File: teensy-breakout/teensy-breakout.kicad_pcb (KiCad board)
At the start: 6 copper layers, 139.7 x 133.4 mm, 80 parts, among them J1 USB_B, J10 Conn_01x04, J11 Conn_01x04, J12 Conn_01x05, J13 Conn_01x03, J14 Conn_01x04, J15 Conn_01x04, J16 Conn_01x02, J17 Conn_01x08, J18 Conn_01x08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

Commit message: Added most of the silkscreen
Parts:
- added G***: LOGO, LOGO, F.Cu at (213.4, 240.0)
- added G***: LOGO, LOGO, F.Cu at (168.9, 212.1)
- added G***: LOGO, LOGO, F.Cu at (189.2, 212.1)
- added REF**: MountingHole_3.2mm_M3, MountingHole:MountingHole_3.2mm_M3, F.Cu at (104.1, 261.6)
- added REF**: MountingHole_3.2mm_M3, MountingHole:MountingHole_3.2mm_M3, F.Cu at (227.3, 172.7)
- added REF**: MountingHole_3.2mm_M3, MountingHole:MountingHole_3.2mm_M3, F.Cu at (227.3, 261.6)
- added REF**: MountingHole_3.2mm_M3, MountingHole:MountingHole_3.2mm_M3, F.Cu at (227.3, 148.6)
- moved J10 5.08 mm to (195.6, 226.1)
- moved J19 3.81 mm to (121.9, 151.1)
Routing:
- net /RC_TX: track 83.8 -> 88.9 mm
- net /RC_RX: track 85.3 -> 90.4 mm
- net /NP1_5V: track 17.1 -> 17.6 mm
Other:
- board text added: "+5V"
- board text added: "4"
- board text added: "5"
- board text added: "GND"
- board text added: "MISO0 12"
- board text added: "MOSI0 11"
- board text added: "SCK0 13"

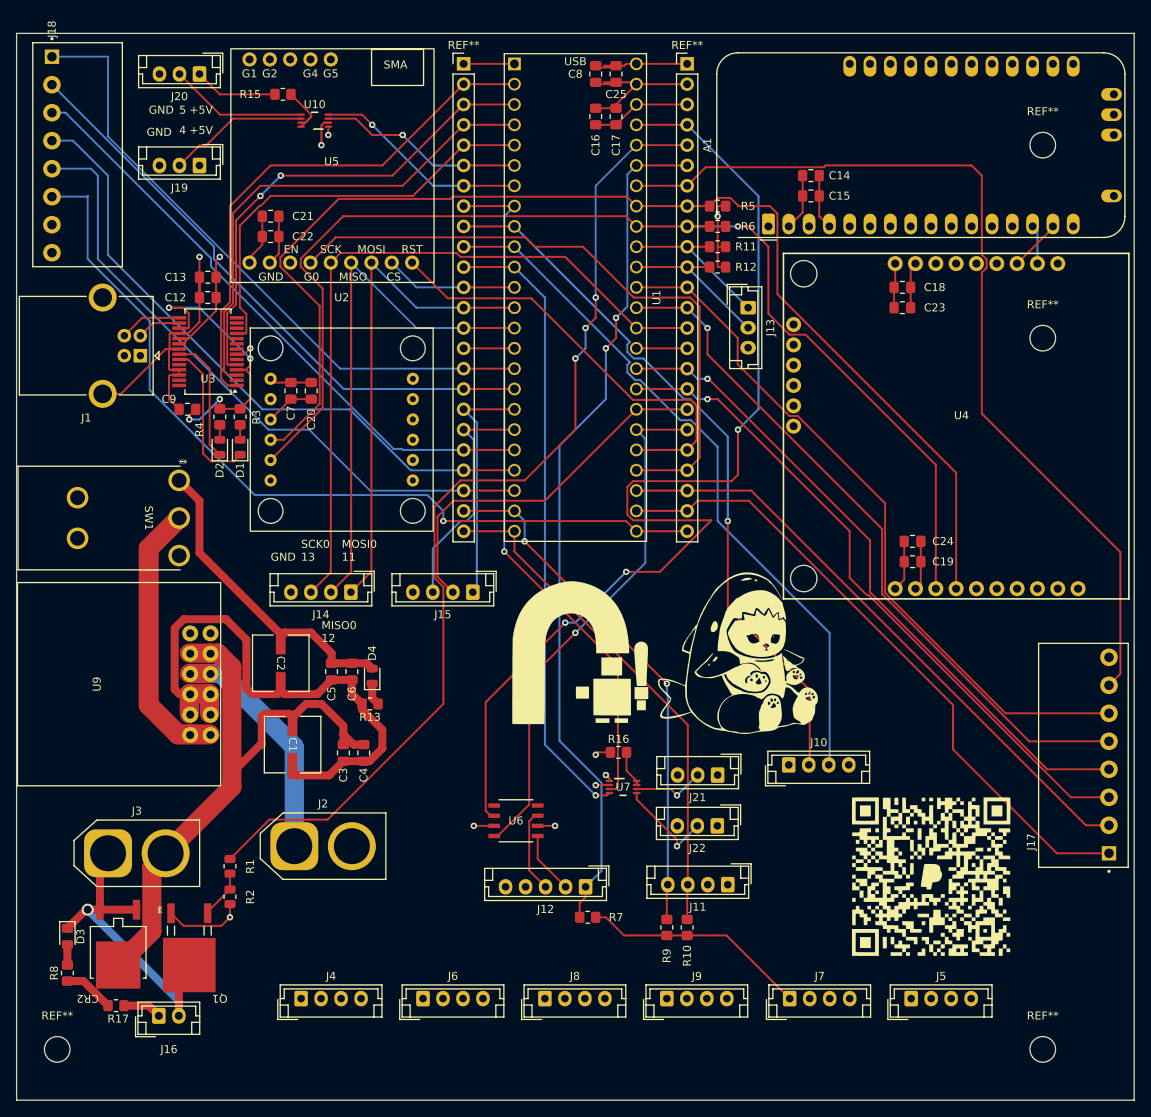
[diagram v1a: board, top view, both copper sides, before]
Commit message: Added rest of silkscreen
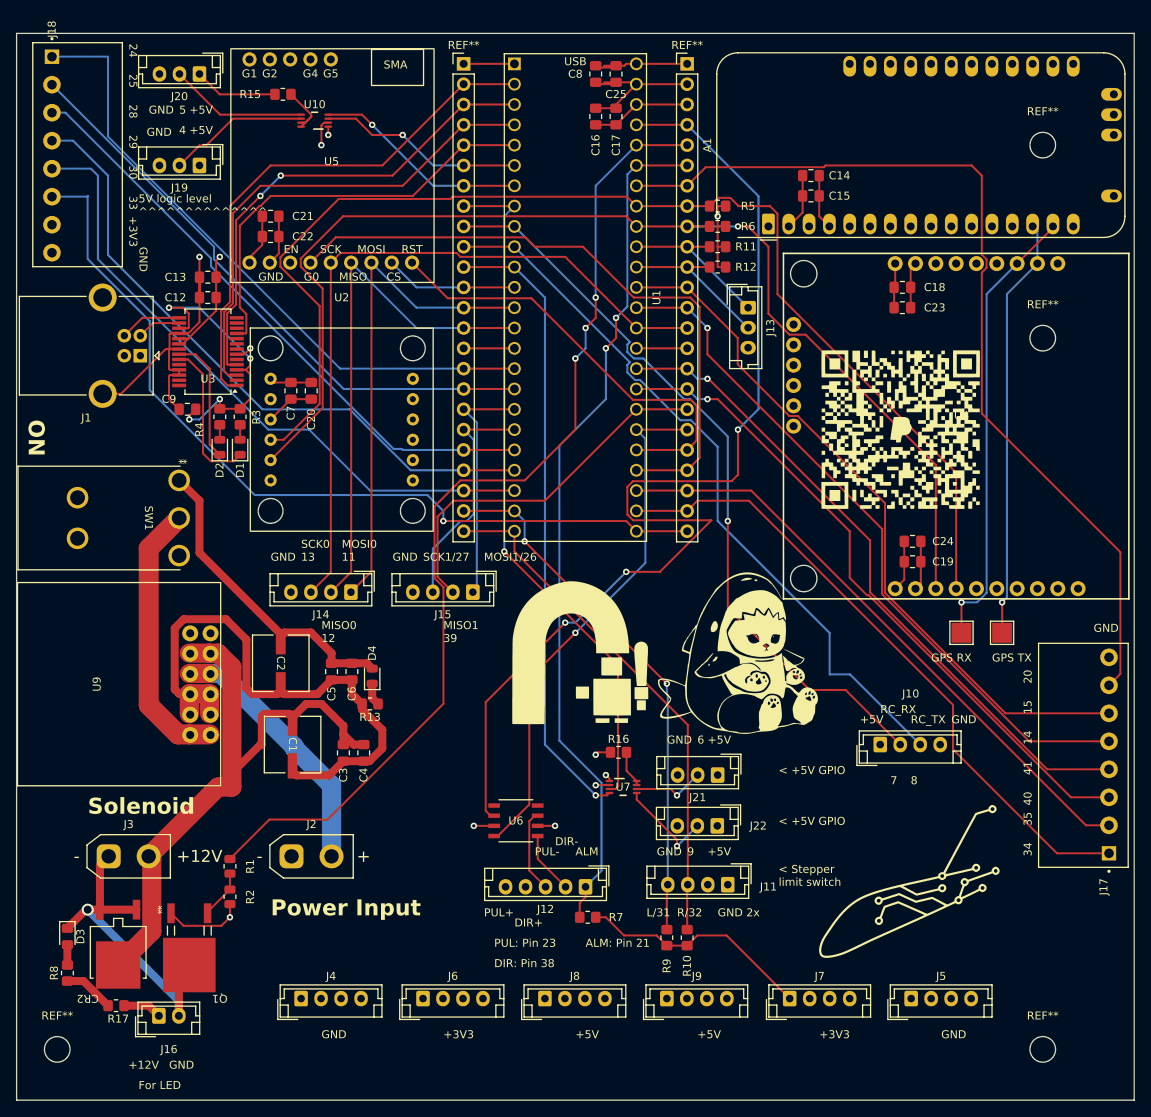
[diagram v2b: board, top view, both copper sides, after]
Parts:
- added G***: LOGO, LOGO, F.Cu at (210.8, 241.3)
- added REF**: TestPoint_Pad_2.5x2.5mm, TestPoint:TestPoint_Pad_2.5x2.5mm, F.Cu at (222.2, 209.6)
- added REF**: TestPoint_Pad_2.5x2.5mm, TestPoint:TestPoint_Pad_2.5x2.5mm, F.Cu at (217.2, 209.6)
- J2, J3: footprint Connector_AMASS:AMASS_XT60-F_1x02_P7.20mm_Vertical -> Connector_AMASS:AMASS_XT30UPB-M_1x02_P5.0mm_Vertical
- moved G*** 56.0 mm to (209.6, 184.2)
- moved J10 11.7 mm to (207.0, 223.5)
- moved J2 1.31 mm to (133.4, 237.5)
- moved R10 1.27 mm to (182.9, 247.7)
- moved R9 1.27 mm to (180.3, 247.7)
- moved J3 0.39 mm to (110.6, 237.5)
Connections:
- J2 pad 1: Net-(J2-Pin_1) -> GND
- J2 pad 2: GND -> Net-(J2-Pin_2)
- U9 pad 4: Net-(J2-Pin_1) -> Net-(J2-Pin_2)
- U9 pad 9: Net-(J2-Pin_1) -> Net-(J2-Pin_2)
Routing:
- net /GPS_RX: track 6.50 -> 56.7 mm, vias 0 -> 1
- net /GPS_TX: track 4.89 -> 52.9 mm, vias 0 -> 1
- net Net-(J2-Pin_2): track 0.00 -> 32.5 mm
- net Net-(J2-Pin_1): track 29.3 -> 0.00 mm
- net /RC_RX: track 90.4 -> 95.2 mm
- net /RC_TX: track 88.9 -> 92.5 mm
- net +12V: track 84.5 -> 85.8 mm
- net /LIM_R: track 63.9 -> 65.2 mm
- net /LIM_L: track 65.4 -> 66.7 mm
- net +3V3: track 89.1 -> 90.2 mm
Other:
- board text added: "+12V"
- board text added: "+3V3"
- board text added: "14"
- board text added: "15"
- board text added: "20"
- board text added: "24"
- board text added: "25"
- board text added: "28"
- board text added: "29"
- board text added: "30"
- board text added: "33"
- board text added: "34"
- board text added: "35"
- board text added: "40"
- board text added: "41"
- board text added: "5V logic level ^^^^^^^^^^^^^^"
- board text added: "6"
- board text added: "7"
- board text added: "8"
- board text added: "9"
- board text added: "< +5V GPIO"
- board text added: "< Stepper limit switch"
- board text added: "ALM"
- board text added: "ALM: Pin 21"
- board text added: "DIR+"
- board text added: "DIR-"
- board text added: "DIR: Pin 38"
- board text added: "For LED"
- board text added: "GND 2x"
- board text added: "GPS RX"
- board text added: "GPS TX"
- board text added: "L/31"
- board text added: "MISO1 39"
- board text added: "MOSI1/26"
- board text added: "ON"
- board text added: "PUL+"
- board text added: "PUL-"
- board text added: "PUL: Pin 23"
- board text added: "Power Input"
- board text added: "R/32"
- board text added: "RC_RX"
- board text added: "RC_TX"
- board text added: "SCK1/27"
- board text added: "Solenoid"

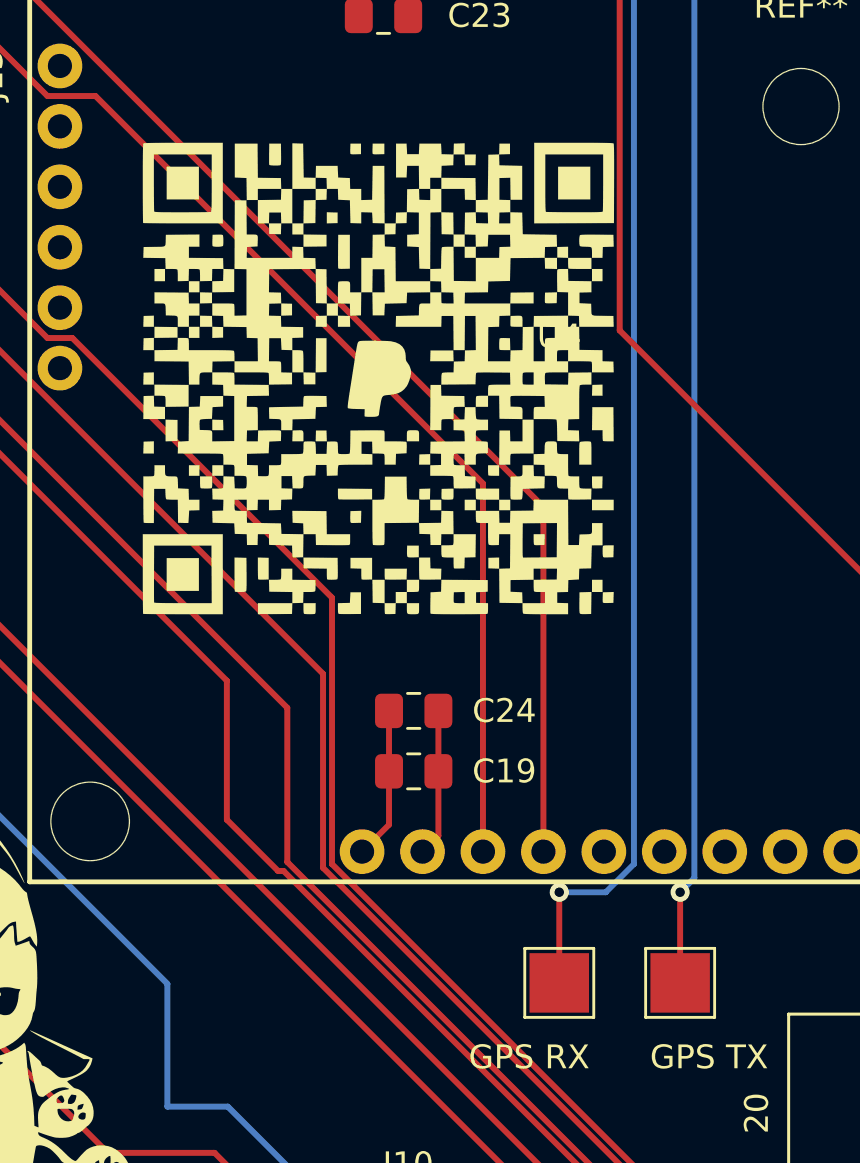
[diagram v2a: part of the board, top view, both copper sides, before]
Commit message: Fixed DRC warnings
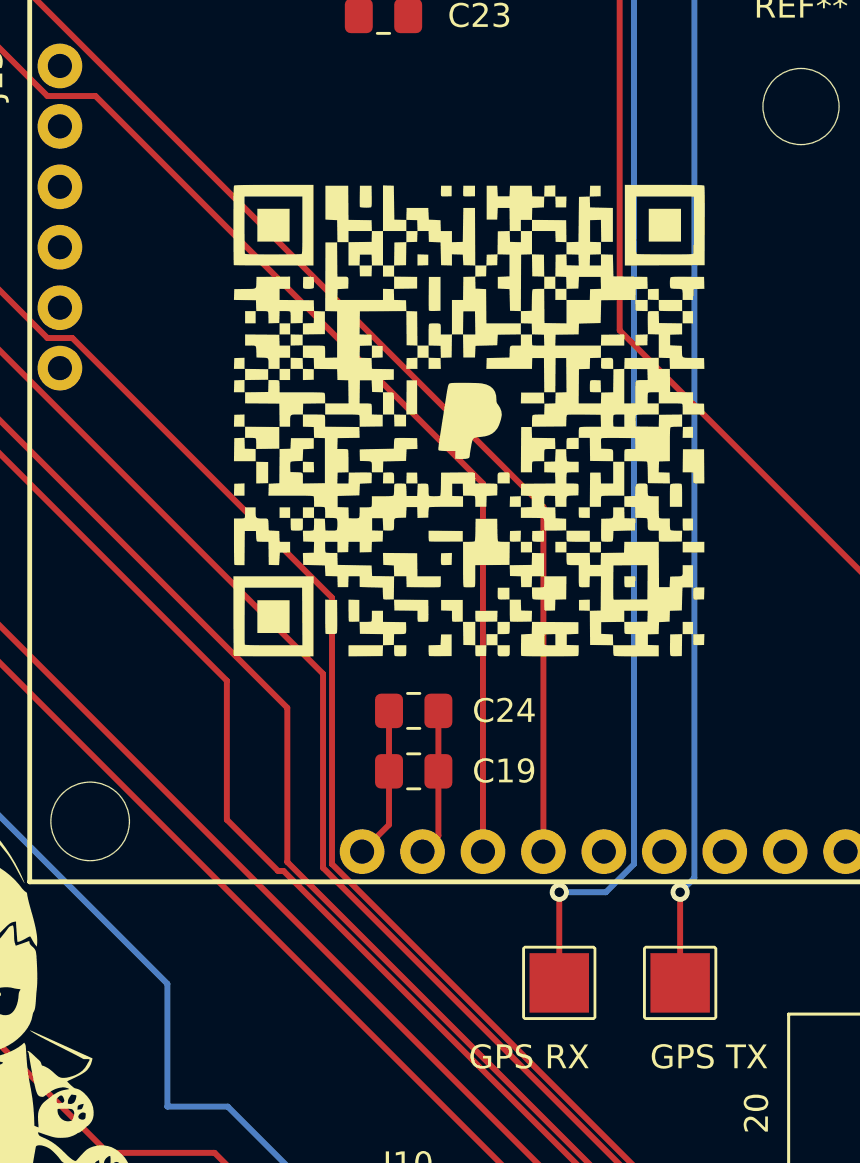
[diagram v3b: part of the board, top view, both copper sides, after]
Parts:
- moved G*** 4.20 mm to (213.4, 185.9)
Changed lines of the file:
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@@
 		(attr exclude_from_pos_files exclude_from_bom)
 		(fp_line
-			(start -1.45 -1.45)
-			(end 1.45 -1.45)
+			(start -1.5 1.45)
+			(end -1.5 -1.45)
 			(stroke
 				(width 0.12)
@@
 		)
 		(fp_line
-			(start -1.45 1.45)
-			(end -1.45 -1.45)
+			(start -1.45 -1.5)
+			(end 1.45 -1.5)
 			(stroke
 				(width 0.12)
@@
 		)
 		(fp_line
-			(start 1.45 -1.45)
-			(end 1.45 1.45)
+			(start 1.45 1.5)
+			(end -1.45 1.5)
 			(stroke
 				(width 0.12)
@@
 		)
 		(fp_line
-			(start 1.45 1.45)
-			(end -1.45 1.45)
+			(start 1.5 -1.45)
+			(end 1.5 1.45)
 			(stroke
 				(width 0.12)
@@
 	(footprint "LOGO"
 		(layer "F.Cu")
-		(at 209.55 184.15)
+		(at 213.36 185.92)
 		(property "Reference" "G***"
 			(at 0 0 0)
@@
 		(at 217.17 182.88)
 		(property "Reference" "U4"
-			(at 0 -0.5 0)
+			(at -3.81 1.27 0)
 			(unlocked yes)
 			(layer "F.SilkS")
+			(hide yes)
 			(effects
 				(font
@@
 		(attr exclude_from_pos_files exclude_from_bom)
 		(fp_line
-			(start -1.45 -1.45)
-			(end 1.45 -1.45)
+			(start -1.5 1.45)
+			(end -1.5 -1.45)
 			(stroke
 				(width 0.12)
@@
 		)
 		(fp_line
-			(start -1.45 1.45)
-			(end -1.45 -1.45)
+			(start -1.45 -1.5)
+			(end 1.45 -1.5)
 			(stroke
 				(width 0.12)
@@
 		)
 		(fp_line
-			(start 1.45 -1.45)
-			(end 1.45 1.45)
+			(start 1.45 1.5)
+			(end -1.45 1.5)
 			(stroke
 				(width 0.12)
@@
 		)
 		(fp_line
-			(start 1.45 1.45)
-			(end -1.45 1.45)
+			(start 1.5 -1.45)
+			(end 1.5 1.45)
 			(stroke
 				(width 0.12)

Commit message: Fix small issue
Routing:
- net +12V: track 85.8 -> 92.3 mm
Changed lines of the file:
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@@
 	)
 	(segment
-		(start 105.41 253.077)
-		(end 107.41 253.077)
+		(start 109.76 253.077)
+		(end 111.76 251.077)
 		(width 1)
 		(layer "F.Cu")
@@
 	)
 	(segment
-		(start 107.41 253.077)
-		(end 110.49 256.157)
+		(start 105.41 253.077)
+		(end 109.76 253.077)
 		(width 1)
 		(layer "F.Cu")
@@
 	)
 	(segment
+		(start 110.49 256.157)
+		(end 110.49 252.347)
+		(width 1)
+		(layer "F.Cu")
+		(net 1)
+	)
+	(segment
 		(start 124.223718 212.09)
 		(end 123.19 212.09)
@@
 		(width 1)
 		(layer "F.Cu")
+		(net 1)
+	)
+	(segment
+		(start 110.49 252.347)
+		(end 111.76 251.077)
+		(width 1)
+		(layer "F.Cu")
